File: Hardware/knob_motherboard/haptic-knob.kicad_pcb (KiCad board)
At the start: 4 copper layers, 50 x 50 mm, 75 parts, among them J1 USB_C_Receptacle_USB2.0, J2 Conn_01x14_Socket, J3 Conn_ARM_SWD_TagConnect_TC203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, M1 BLDC, U1 ESP32-S3-WROOM-1U, U2 PDRV8311HRRWR, U3 MT6701, U4 CH224K, U5 LSM6DSO, U6 MT2492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

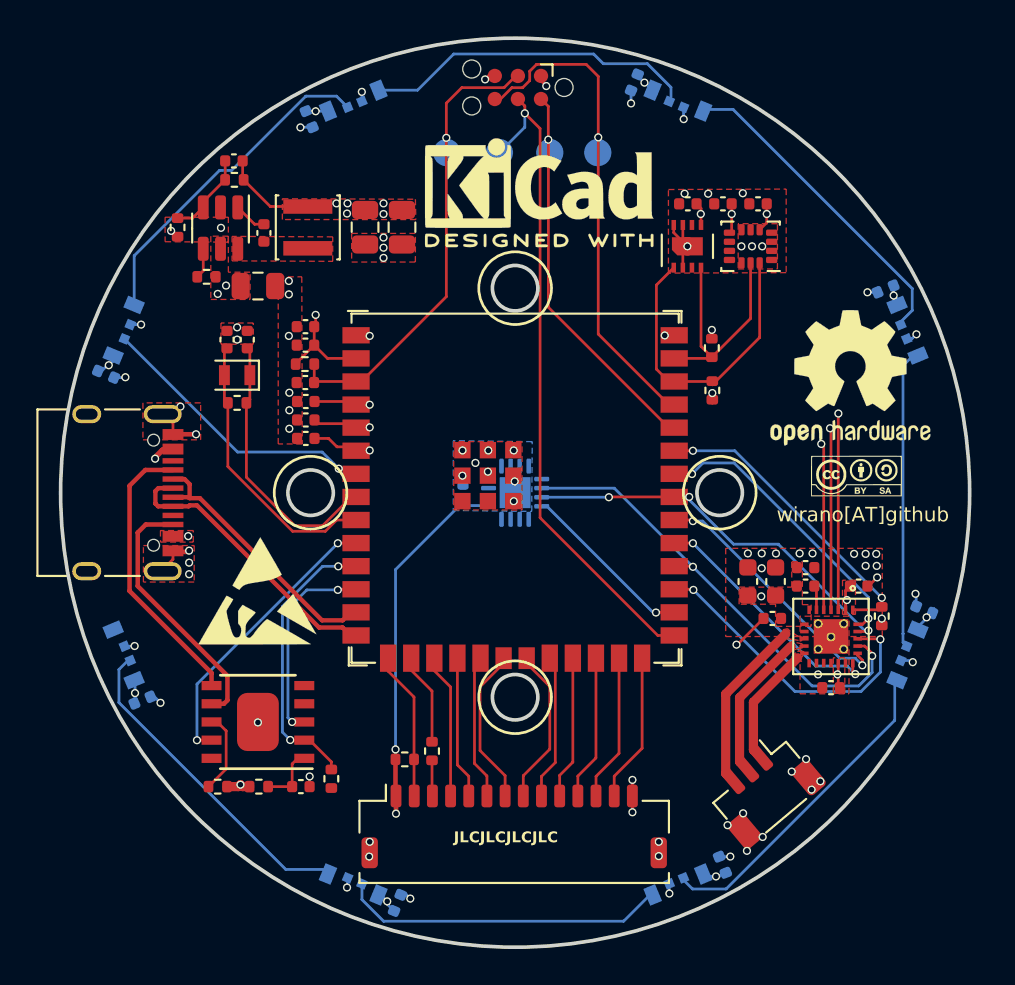
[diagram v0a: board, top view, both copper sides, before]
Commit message: drv8311 spi bugfix & ch224k CFG1 bugfix
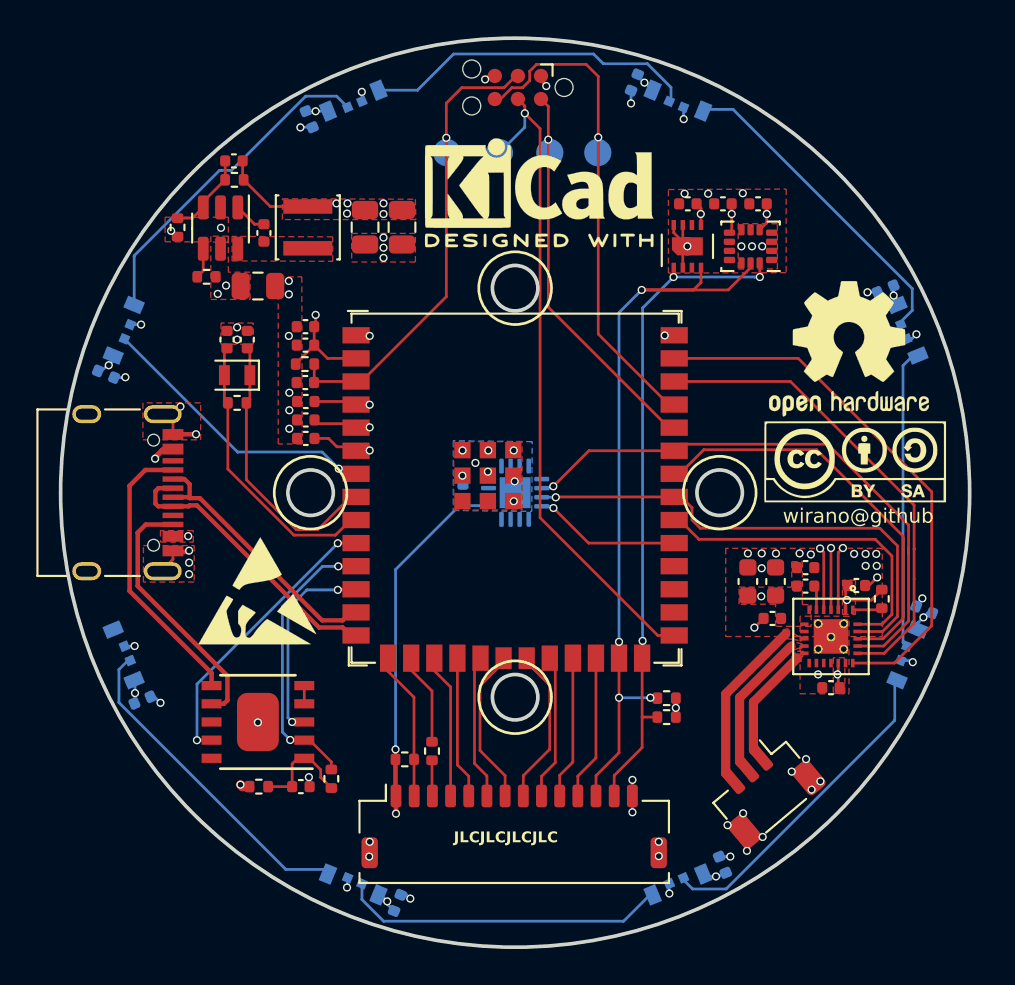
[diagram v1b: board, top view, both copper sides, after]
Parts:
- removed R8: 10K, Resistor_SMD:R_0402_1005Metric
- G***: footprint w_logo:Logo_silk_CC-BY-SA_5x2mm -> w_logo:Logo_silk_CC-BY-SA_10x4.5mm
- moved R14 19.4 mm to (123.3, 144.2), turned to 180 degrees
- moved R13 18.1 mm to (123.3, 145.2), turned to 180 degrees
- moved REF** 1.60 mm to (133.3, 125.0)
- moved R6 0.95 mm to (135.1, 138.7), turned to 90 degrees
- moved G*** 0.79 mm to (133.6, 131.2)
- moved C20 0.13 mm to (133.7, 138.0)
- turned R3 to 90 degrees
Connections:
- R13 pad 2: /Sensor/SDA -> /Core/TP_SDA
- R14 pad 2: /Sensor/SCL -> /Core/TP_SCL
- R3 pad 1: /Core/CFG1 -> Net-(U4-VDD)
- R3 pad 2: +3.3V -> /Core/CFG1
- R6 pad 1: /BLDC/nFAULT -> Net-(U2-FAULT_N)
- U1 pad 28: /BLDC/ENC_CS -> unconnected-(U1-SPIIO6/GPIO35/FSPID/SUBSPID-Pad28)
- U1 pad 29: /BLDC/SDI -> unconnected-(U1-SPIIO7/GPIO36/FSPICLK/SUBSPICLK-Pad29)
- U1 pad 30: /BLDC/SDO -> unconnected-(U1-SPIDQS/GPIO37/FSPIQ/SUBSPIQ-Pad30)
- U1 pad 31: /BLDC/PWM_SYNC -> /BLDC/ENC_CS
- U1 pad 32: /BLDC/DRV_CS -> /BLDC/nSLEEP
- U1 pad 34: /BLDC/nSLEEP -> /BLDC/SDI
- U1 pad 35: /BLDC/nFAULT -> /BLDC/SDO
- U1 pad 38: /Sensor/SDA -> /BLDC/DRV_CS
- U1 pad 39: /Sensor/SCL -> /BLDC/PWM_SYNC
- U2 pad 1: /BLDC/nFAULT -> Net-(U2-FAULT_N)
- U4 pad 4: unconnected-(U4-DP-Pad4) -> Net-(U4-DM)
- U4 pad 5: unconnected-(U4-DM-Pad5) -> Net-(U4-DM)
- U4 pad 8: Net-(U4-VBUS) -> unconnected-(U4-VBUS-Pad8)
- U5 pad 13: /Sensor/SCL -> /Core/TP_SCL
- U5 pad 14: /Sensor/SDA -> /Core/TP_SDA
- U7 pad 1: /Sensor/SDA -> /Core/TP_SDA
- U7 pad 4: /Sensor/SCL -> /Core/TP_SCL
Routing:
- net /Core/TP_SCL: track 8.10 -> 42.0 mm, vias 0 -> 4
- net /Core/TP_SDA: track 8.22 -> 36.8 mm, vias 0 -> 3
- net /Sensor/SDA: track 17.2 -> 0.00 mm
- net /BLDC/nFAULT: track 16.9 -> 0.00 mm, vias 2 -> 0
- net /BLDC/PWM_SYNC: track 13.6 -> 29.8 mm, vias 2 -> 0
- net /Sensor/SCL: track 13.3 -> 0.00 mm
- net /BLDC/DRV_CS: track 14.4 -> 26.3 mm, vias 2 -> 0
- net /BLDC/SDO: track 26.0 -> 32.0 mm, vias 2 -> 1
- net /BLDC/SCLK: track 21.7 -> 27.5 mm, vias 3 -> 1
- net /BLDC/SDI: track 17.2 -> 22.6 mm, vias 2 -> 0
- net Net-(U4-VBUS): track 4.48 -> 0.00 mm
- net /Core/SOA: track 37.3 -> 33.9 mm
- net /Core/SOB: track 38.4 -> 35.2 mm
- net /Core/SOC: track 39.6 -> 36.4 mm
- net Net-(U4-VDD): track 3.36 -> 5.78 mm
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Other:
- board text added: "wirano@github"
- board text removed: "wirano[AT]github"
